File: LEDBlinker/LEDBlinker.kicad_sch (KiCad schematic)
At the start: 0 parts

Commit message: Created initial schematic for LED blinker
includes IO, lights, switches, inversion and spot for timer
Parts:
- added D1, D2, D3, D4, D5, D6: LED, symbol Device:LED
- added J1: Conn_01x02_Pin, symbol Connector:Conn_01x02_Pin
- added Q1, Q2, Q3: 2N7000, Package_TO_SOT_THT:TO-92_Inline, symbol Transistor_FET:2N7000
- added R1, R2, R3, R4, R5, R6, R7: R_US, symbol Device:R_US
- added SW1: SW_SPDT, symbol Switch:SW_SPDT
- added U1: ICM7555xP, Package_DIP:DIP-8_W7.62mm, symbol Timer:ICM7555xP
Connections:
- new net: Q2.3 (D), R7.2, SW1.2 (B)
- new net: D4.2 (A), R4.2
- new net: D2.2 (A), R2.2
- new net: Q1.1 (S), R1.1, R2.1, R3.1
- new net: D5.2 (A), R5.2
- new net: D1.2 (A), R1.2
- new net: D3.2 (A), R3.2
- new net: Q3.1 (S), R4.1, R5.1, R6.1
- new net: D6.2 (A), R6.2
- new net +5V: J1.1 (Pin_1), Q1.3 (D), Q3.3 (D), R7.1, U1.8 (VCC)
- new net GND: D1.1 (K), D2.1 (K), D3.1 (K), D4.1 (K), D5.1 (K), D6.1 (K), J1.2 (Pin_2), Q2.1 (S), U1.1 (GND)
- new net Inv_Out: Q3.2 (G), SW1.1 (A)
- new net T_Out: Q1.2 (G), Q2.2 (G), U1.3 (OUT)

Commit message: Initial Commit
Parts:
- removed D1, D2: LED, symbol Device:LED
- removed J1: Conn_01x02_Pin, symbol Connector:Conn_01x02_Pin
- removed Q1, Q2, Q3: 2N7000, Package_TO_SOT_THT:TO-92_Inline, symbol Transistor_FET:2N7000
- removed R3, R4, R5, R6, R7: R_US, symbol Device:R_US
- removed SW1: SW_SPDT, symbol Switch:SW_SPDT
- removed U1: ICM7555xP, Package_DIP:DIP-8_W7.62mm, symbol Timer:ICM7555xP
- added C1, C2: C, symbol Device:C
- added D10, D7: LED, symbol Device:LED
- added J1: USB-C Breakout, symbol Connector_Generic:Conn_01x06
- added R8, R9: R_US, symbol Device:R_US
- added SW2: SW_SPST, symbol Switch:SW_SPST
- added U1: CD4017BE, N16, symbol CD4017BE:CD4017BE
- added U2: LM555xN, Package_DIP:DIP-8_W7.62mm, symbol Timer:LM555xN
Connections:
- net +5V: now also R1.1, J1.1 (Pin_1), SW2.1 (A), U1.16 (VDD), U2.4 (~{RST}), U2.8 (VCC)
- net GND: now also C1.2, C2.2, J1.2 (Pin_2), R8.1, R9.1, U1.13 (CLOCKINHIBIT), U1.8 (VSS), U2.1 (GND); no longer D3.1 (K), D4.1 (K), D5.1 (K), D6.1 (K)
- net at D4.2 (A): now also U1.10 (4)
- net at R2.2: now also C1.1, U2.2 (TRIG), U2.6 (THRES)
- net at R2.1: now also R1.2, U2.7 (DISCH); no longer R1.1
- net at D5.2 (A): now also U1.1 (5)
- net at D3.2 (A): now also U1.7 (3)
- net at D6.2 (A): now also U1.4 (2)
- new net: D10.1 (K), D3.1 (K), D4.1 (K), D5.1 (K), D6.1 (K), D7.1 (K), R9.2
- new net: D10.2 (A), U1.3 (0)
- new net: D7.2 (A), U1.2 (1)
- new net: C2.1, U2.5 (CONT)
- new net: R8.2, SW2.2 (B), U1.15 (RESET), U1.5 (6)
- new net OUT: U1.14 (CLOCK), U2.3 (OUT)
- no-connect marks 0 -> 8
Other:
- note added: "555 Timer"
- note added: "LED Chaser"
- note added: "USB-C Breakout"

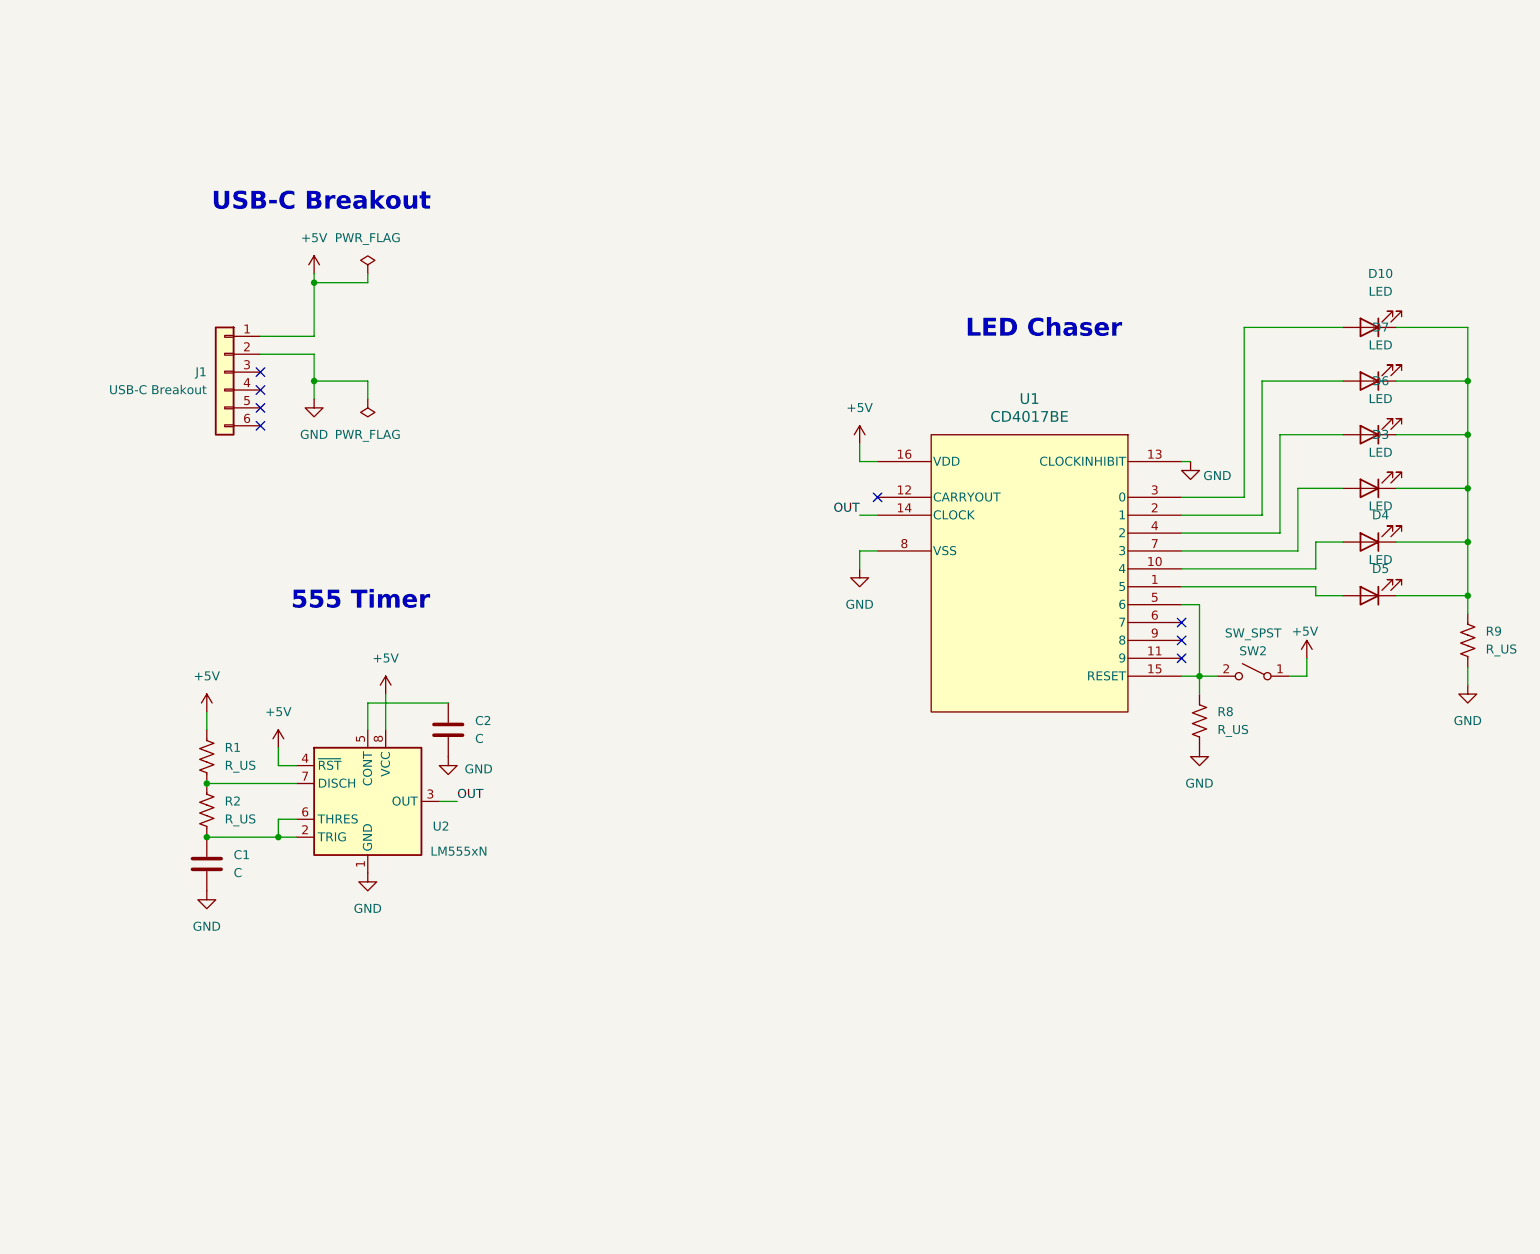
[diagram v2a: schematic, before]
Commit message: Add KiCad PCB, parts, footprints and backups
Add a full KiCad PCB file (LEDBlinker.kicad_pcb) with multiple LED footprints, mounting holes and models, and update related project files (.kicad_prl, .kicad_pro, .kicad_sch). Add several backup ZIPs under LEDBlinker/LEDBlinker-backups and multiple new part libraries and footprint files (PT01_D115D_B104, SLW_883935_2A_D, treedix-usb-c-breakout-board, ul_CD4017BE, N0016A, etc.). Update fp-lib-table and sym-lib-table to include the new resources and remove the stale schematic lock file.
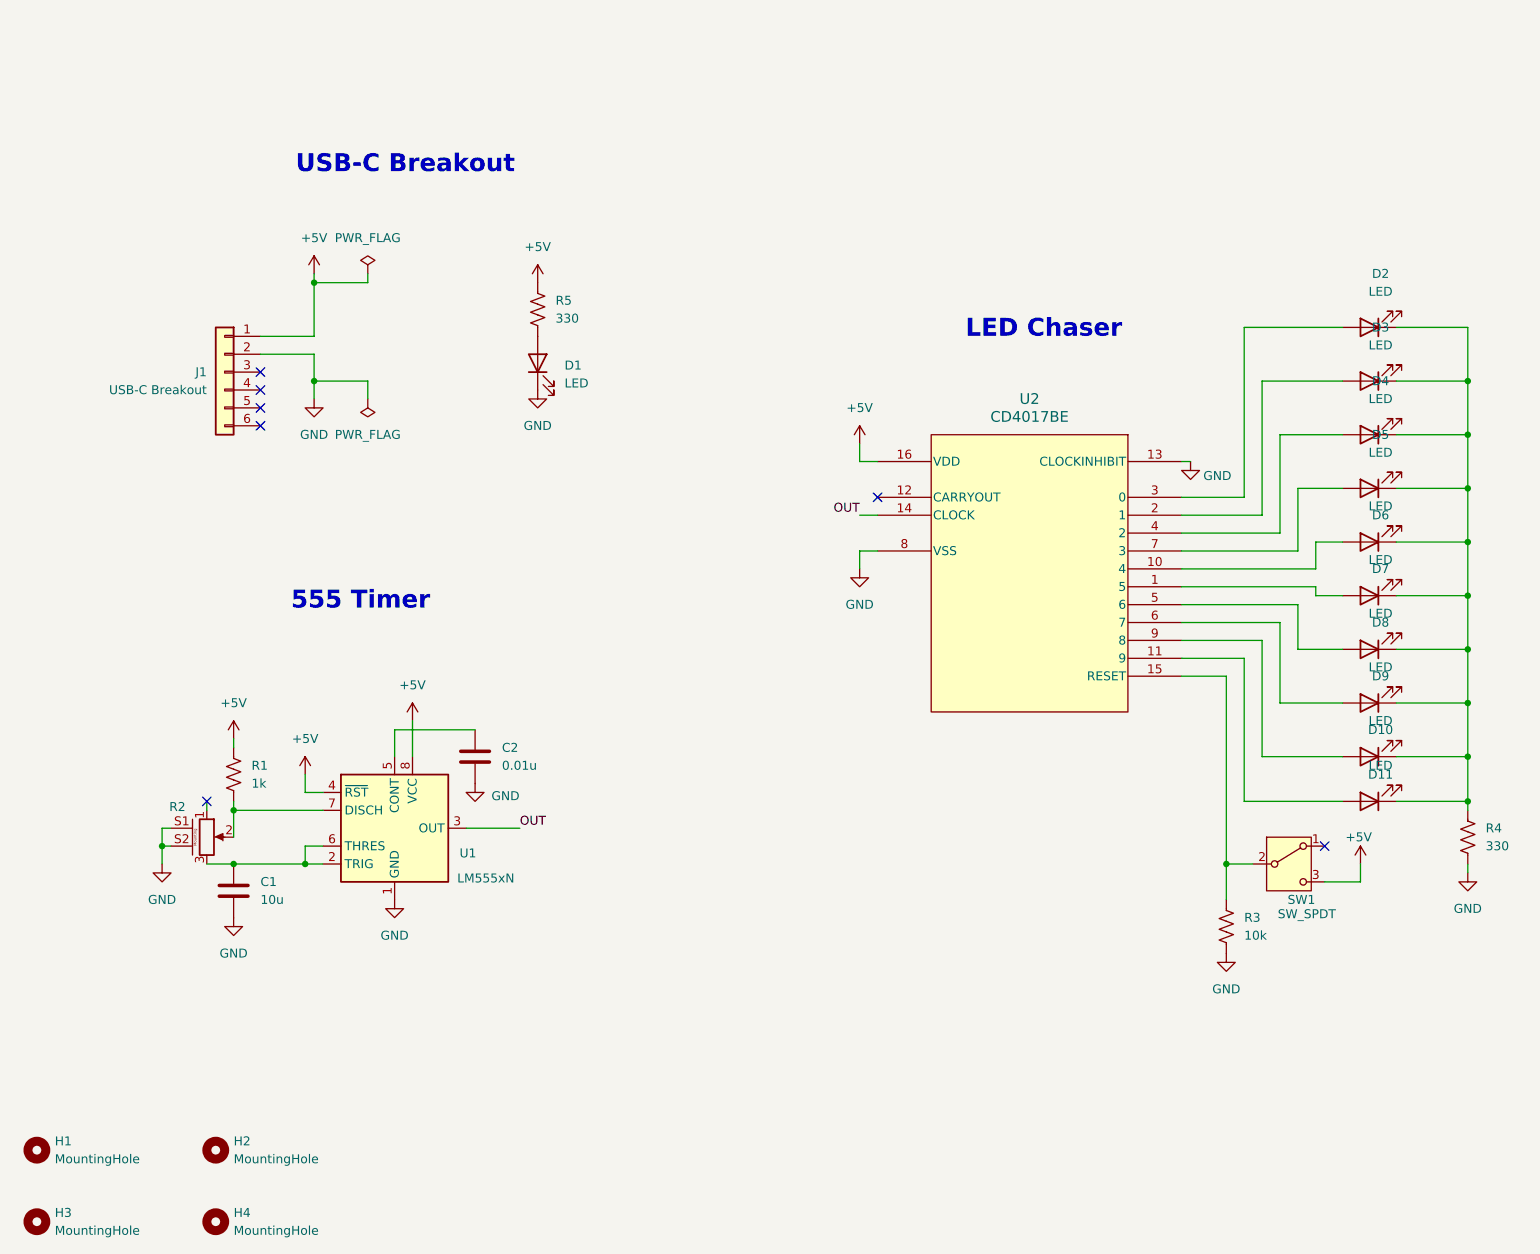
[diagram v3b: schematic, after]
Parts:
- removed R2: R_US, symbol Device:R_US
- removed SW2: SW_SPST, symbol Switch:SW_SPST
- added D1, D10, D11, D8, D9: LED, LED_THT:LED_D5.0mm_Clear, symbol Device:LED
- added H1, H2, H3, H4: MountingHole, MountingHole:MountingHole_2.2mm_M2_DIN965, symbol Mechanical:MountingHole
- added R2: PT01-D115D-B104, PT01_D115D_B104:TRIM_PT01-D115D-B104, symbol PT01-D115D-B104:PT01-D115D-B104
- added R5: 330, Resistor_THT:R_Axial_DIN0207_L6.3mm_D2.5mm_P10.16mm_Horizontal, symbol Device:R_US
- added SW1: SW_SPDT, SLW_883935_2A_D:SW_SLW-883935-2A-D, symbol Switch:SW_SPDT
- C1: value C -> 10u; footprint (none) -> Capacitor_THT:CP_Radial_D5.0mm_P2.00mm
- C2: value C -> 0.01u; footprint (none) -> Capacitor_THT:C_Disc_D6.0mm_W4.4mm_P5.00mm
- D2: renamed from D10; footprint (none) -> LED_THT:LED_D5.0mm_Clear
- D3: renamed from D7; footprint (none) -> LED_THT:LED_D5.0mm_Clear
- D4: renamed from D6; footprint (none) -> LED_THT:LED_D5.0mm_Clear
- D5: renamed from D3; footprint (none) -> LED_THT:LED_D5.0mm_Clear
- D6: renamed from D4; footprint (none) -> LED_THT:LED_D5.0mm_Clear
- D7: renamed from D5; footprint (none) -> LED_THT:LED_D5.0mm_Clear
- J1: footprint (none) -> treedix-usb-c-breakout-board:PinHeader_1x06_P2.54mm_Vertical
- R1: value R_US -> 1k; footprint (none) -> Resistor_THT:R_Axial_DIN0207_L6.3mm_D2.5mm_P10.16mm_Horizontal
- R3: renamed from R8; value R_US -> 10k; footprint (none) -> Resistor_THT:R_Axial_DIN0207_L6.3mm_D2.5mm_P10.16mm_Horizontal
- R4: renamed from R9; value R_US -> 330; footprint (none) -> Resistor_THT:R_Axial_DIN0207_L6.3mm_D2.5mm_P10.16mm_Horizontal
- U2: renamed from U1; footprint N16 -> CD4017BE:N16
- renumbered U2 to U1
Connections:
- net +5V: now also R5.1, SW1.3 (C)
- net GND: now also D1.1 (K), R2.S1 (MountPin), R2.S2 (MountPin)
- net at R1.2, U1.7 (DISCH): now also R2.2
- net at D2.1 (K), D3.1 (K), D4.1 (K)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: now also D10.1 (K), D11.1 (K), D8.1 (K), D9.1 (K)
- net at C1.1, U1.2 (TRIG), U1.6 (THRES): now also R2.3
- net at R3.2, U2.15 (RESET): now also SW1.2 (B); no longer U2.5 (6)
- net at U2.11 (9): now also D11.2 (A)
- net at U2.6 (7): now also D9.2 (A)
- net at U2.9 (8): now also D10.2 (A)
- new net: D8.2 (A), U2.5 (6)
- new net: D1.2 (A), R5.2
- no-connect marks 8 -> 7
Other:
- moved on the sheet: C1, C2, R1, R3, R4, U1

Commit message: Final commit before purchase
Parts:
- C1: footprint Capacitor_THT:CP_Radial_D5.0mm_P2.00mm -> Capacitor_THT:CP_Radial_D5.0mm_P2.50mm
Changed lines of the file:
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@@
 			)
 		)
-		(property "Footprint" "Capacitor_THT:CP_Radial_D5.0mm_P2.00mm"
+		(property "Footprint" "Capacitor_THT:CP_Radial_D5.0mm_P2.50mm"
 			(at 54.3052 144.78 0)
 			(hide yes)
